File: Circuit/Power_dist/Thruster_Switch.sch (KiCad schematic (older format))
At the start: 11 parts, among them P1 XT60, P2 XT60, P3 XT60, P4 XT60, Q1 IPD90P03P4L

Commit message: edit sch and add pcix16
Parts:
- removed P2, P3, P4: XT60, zeabus:XT60, symbol XT60
- Q1: footprint TO_SOT_Packages_SMD:TO-252-2Lead -> TO_SOT_Packages_SMD:TO-252-2
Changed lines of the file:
@@
 EESchema Schematic File Version 2
+LIBS:Power_Distributor-rescue
 LIBS:power
 LIBS:device
@@
 LIBS:zeabus
 LIBS:ftdi
+LIBS:Power_Distributor-cache
 EELAYER 25 0
 EELAYER END
 $Descr A4 11693 8268
 encoding utf-8
-Sheet 6 9
+Sheet 2 9
 Title "Thruster Switch"
 Date "2017-04-06"
@@
 AR Path="/58E62AD5/58E019DD" Ref="P7"  Part="1"
 AR Path="/58E0048C/58E019DD" Ref="P11"  Part="1"
-F 0 "P11" H 6850 4450 50  0000 C CNN
+F 0 "P1" H 6850 4450 50  0000 C CNN
 F 1 "XT60" H 6850 4150 50  0000 C CNN
 F 2 "zeabus:XT60" H 6950 4050 60  0001 C CNN
@@
 AR Path="/58E62AD5/58E01A68" Ref="R12"  Part="1"
 AR Path="/58E0048C/58E01A68" Ref="R15"  Part="1"
-F 0 "R15" V 6330 4150 50  0000 C CNN
+F 0 "R3" V 6330 4150 50  0000 C CNN
 F 1 "10k" V 6250 4150 50  0000 C CNN
 F 2 "Resistors_SMD:R_0603" V 6180 4150 50  0001 C CNN
@@
 AR Path="/58E62AD5/58E01A8B" Ref="D8"  Part="1"
 AR Path="/58E0048C/58E01A8B" Ref="D10"  Part="1"
-F 0 "D10" H 6200 4675 50  0000 L CNN
+F 0 "D2" H 6200 4675 50  0000 L CNN
 F 1 "LED_Small" H 6075 4450 50  0000 L CNN
 F 2 "LEDs:LED_0603" V 6250 4550 50  0001 C CNN
@@
 AR Path="/58E62AD5/58E01FA8" Ref="R10"  Part="1"
 AR Path="/58E0048C/58E01FA8" Ref="R13"  Part="1"
-F 0 "R13" V 5630 2500 50  0000 C CNN
+F 0 "R1" V 5630 2500 50  0000 C CNN
 F 1 "10k" V 5550 2500 50  0000 C CNN
 F 2 "Resistors_SMD:R_0603" V 5480 2500 50  0001 C CNN
@@
 AR Path="/58E62AD5/58E01FFB" Ref="R11"  Part="1"
 AR Path="/58E0048C/58E01FFB" Ref="R14"  Part="1"
-F 0 "R14" V 5630 3050 50  0000 C CNN
+F 0 "R2" V 5630 3050 50  0000 C CNN
 F 1 "2.2k" V 5550 3050 50  0000 C CNN
 F 2 "Resistors_SMD:R_0603" V 5480 3050 50  0001 C CNN
@@
 $EndComp
 $Comp
-L GND #PWR011
+L GND #PWR020
 U 1 1 58E0369B
 P 6250 4800
-AR Path="/58E52973/58E0369B" Ref="#PWR011"  Part="1"
-AR Path="/58E62AD5/58E0369B" Ref="#PWR014"  Part="1"
-AR Path="/58E0048C/58E0369B" Ref="#PWR015"  Part="1"
-F 0 "#PWR015" H 6250 4550 50  0001 C CNN
+AR Path="/58E52973/58E0369B" Ref="#PWR020"  Part="1"
+AR Path="/58E62AD5/58E0369B" Ref="#PWR023"  Part="1"
+AR Path="/58E0048C/58E0369B" Ref="#PWR024"  Part="1"
+F 0 "#PWR024" H 6250 4550 50  0001 C CNN
 F 1 "GND" H 6250 4650 50  0000 C CNN
 F 2 "" H 6250 4800 50  0001 C CNN
@@
 Text HLabel 3700 3050 0    60   Input ~ 0
 Software_Switch
-$Comp
-L XT60 P2
-U 1 1 58E0D2A0
-P 7400 4300
-AR Path="/58E52973/58E0D2A0" Ref="P2"  Part="1"
-AR Path="/58E62AD5/58E0D2A0" Ref="P8"  Part="1"
-AR Path="/58E0048C/58E0D2A0" Ref="P12"  Part="1"
-F 0 "P12" H 7400 4450 50  0000 C CNN
-F 1 "XT60" H 7400 4150 50  0000 C CNN
-F 2 "zeabus:XT60" H 7500 4050 60  0001 C CNN
-F 3 "" H 7400 4300 60  0000 C CNN
-	1    7400 4300
-	1    0    0    -1
-$EndComp
-$Comp
-L XT60 P3
-U 1 1 58E0D2E8
-P 7950 4300
-AR Path="/58E52973/58E0D2E8" Ref="P3"  Part="1"
-AR Path="/58E62AD5/58E0D2E8" Ref="P9"  Part="1"
-AR Path="/58E0048C/58E0D2E8" Ref="P13"  Part="1"
-F 0 "P13" H 7950 4450 50  0000 C CNN
-F 1 "XT60" H 7950 4150 50  0000 C CNN
-F 2 "zeabus:XT60" H 8050 4050 60  0001 C CNN
-F 3 "" H 7950 4300 60  0000 C CNN
-	1    7950 4300
-	1    0    0    -1
-$EndComp
-$Comp
-L XT60 P4
-U 1 1 58E0D33F
-P 8500 4300
-AR Path="/58E52973/58E0D33F" Ref="P4"  Part="1"
-AR Path="/58E62AD5/58E0D33F" Ref="P10"  Part="1"
-AR Path="/58E0048C/58E0D33F" Ref="P14"  Part="1"
-F 0 "P14" H 8500 4450 50  0000 C CNN
-F 1 "XT60" H 8500 4150 50  0000 C CNN
-F 2 "zeabus:XT60" H 8600 4050 60  0001 C CNN
-F 3 "" H 8500 4300 60  0000 C CNN
-	1    8500 4300
-	1    0    0    -1
-$EndComp
 $Comp
 L Fuse F1
@@
 AR Path="/58E62AD5/58E4FE30" Ref="F4"  Part="1"
 AR Path="/58E0048C/58E4FE30" Ref="F5"  Part="1"
-F 0 "F5" V 6330 3550 50  0000 C CNN
+F 0 "F1" V 6330 3550 50  0000 C CNN
 F 1 "Fuse" V 6175 3550 50  0000 C CNN
 F 2 "zeabus:FUSE_AUTO" V 6180 3550 50  0001 C CNN
@@
 $EndComp
 Wire Wire Line
-	6250 3850 8300 3850
-Wire Wire Line
 	6650 3850 6650 4250
 Connection ~ 6250 3850
@@
 	5250 2500 5400 2500
 Connection ~ 5250 3050
-Wire Wire Line
-	8300 3850 8300 4250
 Connection ~ 6650 3850
-Wire Wire Line
-	8300 4750 8300 4350
-Wire Wire Line
-	7200 4250 7200 3850
-Connection ~ 7200 3850
-Wire Wire Line
-	7750 4250 7750 3850
-Connection ~ 7750 3850
 Wire Wire Line
 	6250 4450 6250 4300
 Connection ~ 6650 4750
-Wire Wire Line
-	7750 4750 7750 4350
-Connection ~ 7750 4750
-Wire Wire Line
-	7200 4750 7200 4350
-Connection ~ 7200 4750
 Wire Wire Line
 	6250 4650 6250 4800
@@
 AR Path="/58E62AD5/58E51C6A" Ref="Q4"  Part="1"
 AR Path="/58E0048C/58E51C6A" Ref="Q5"  Part="1"
-F 0 "Q5" H 6350 3100 50  0000 L CNN
+F 0 "Q1" H 6350 3100 50  0000 L CNN
 F 1 "IPD90P03P4L" H 6350 3000 50  0000 L CNN
-F 2 "TO_SOT_Packages_SMD:TO-252-2Lead" H 6350 3150 50  0001 C CNN
+F 2 "TO_SOT_Packages_SMD:TO-252-2" H 6350 3150 50  0001 C CNN
 F 3 "" H 6150 3050 50  0001 C CNN
 	1    6150 3050
@@
 AR Path="/58E62AD5/58E6427A" Ref="D7"  Part="1"
 AR Path="/58E0048C/58E6427A" Ref="D9"  Part="1"
-F 0 "D9" H 5850 2850 50  0000 C CNN
+F 0 "D1" H 5850 2850 50  0000 C CNN
 F 1 "BZX585-C12" H 5850 2650 50  0000 C CNN
 F 2 "Diodes_SMD:D_SOD-523" H 5850 2750 50  0001 C CNN
@@
 	5850 2900 5850 3050
 Connection ~ 5850 3050
-Wire Wire Line
-	6250 4750 8300 4750
 Connection ~ 6250 4750
 Wire Wire Line
@@
 Wire Wire Line
 	3700 2300 6250 2300
+Wire Wire Line
+	6250 4750 6650 4750
+Wire Wire Line
+	6650 3850 6250 3850
 $EndSCHEMATC

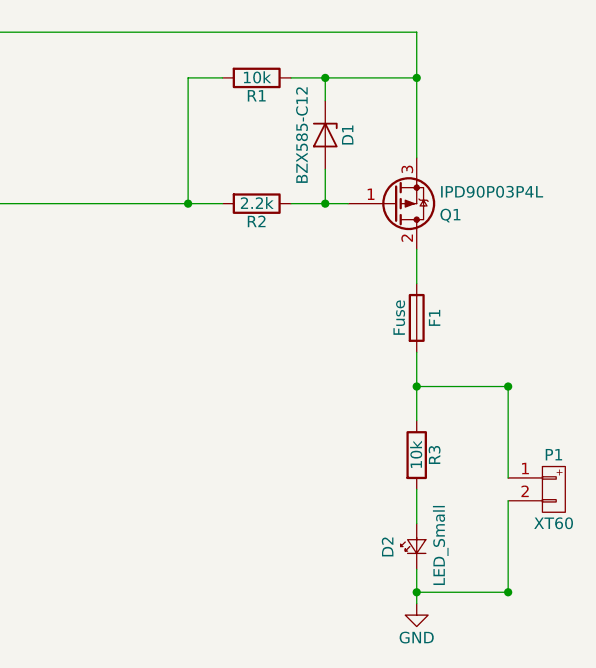
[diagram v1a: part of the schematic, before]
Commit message: delete fuses at thrusters and oring + add power on jumper
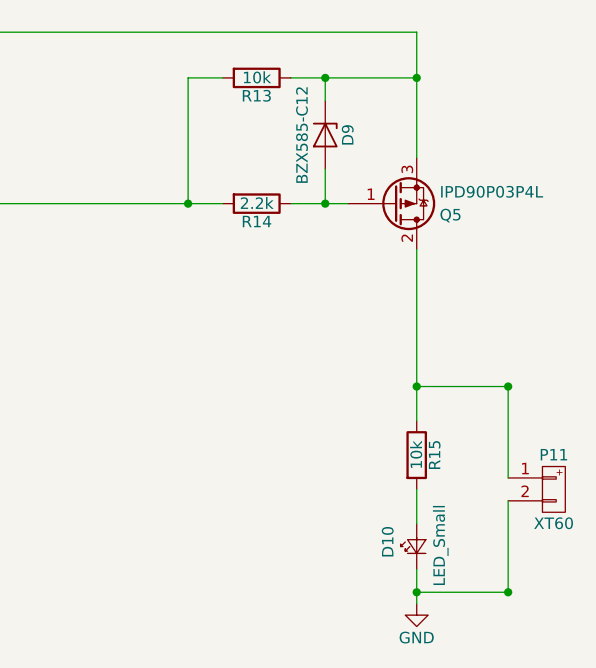
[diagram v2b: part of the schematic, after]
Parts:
- removed F1: Fuse, zeabus:FUSE_AUTO, symbol Fuse
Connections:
- net at P1.1 (P1), R3.1: now also Q1.2 (D)
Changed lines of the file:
@@
 $Descr A4 11693 8268
 encoding utf-8
-Sheet 2 9
+Sheet 5 8
 Title "Thruster Switch"
 Date "2017-04-06"
@@
 AR Path="/58E62AD5/58E019DD" Ref="P7"  Part="1"
 AR Path="/58E0048C/58E019DD" Ref="P11"  Part="1"
-F 0 "P1" H 6850 4450 50  0000 C CNN
+F 0 "P11" H 6850 4450 50  0000 C CNN
 F 1 "XT60" H 6850 4150 50  0000 C CNN
 F 2 "zeabus:XT60" H 6950 4050 60  0001 C CNN
@@
 AR Path="/58E62AD5/58E01A68" Ref="R12"  Part="1"
 AR Path="/58E0048C/58E01A68" Ref="R15"  Part="1"
-F 0 "R3" V 6330 4150 50  0000 C CNN
+F 0 "R15" V 6330 4150 50  0000 C CNN
 F 1 "10k" V 6250 4150 50  0000 C CNN
 F 2 "Resistors_SMD:R_0603" V 6180 4150 50  0001 C CNN
@@
 AR Path="/58E62AD5/58E01A8B" Ref="D8"  Part="1"
 AR Path="/58E0048C/58E01A8B" Ref="D10"  Part="1"
-F 0 "D2" H 6200 4675 50  0000 L CNN
+F 0 "D10" H 6200 4675 50  0000 L CNN
 F 1 "LED_Small" H 6075 4450 50  0000 L CNN
 F 2 "LEDs:LED_0603" V 6250 4550 50  0001 C CNN
@@
 AR Path="/58E62AD5/58E01FA8" Ref="R10"  Part="1"
 AR Path="/58E0048C/58E01FA8" Ref="R13"  Part="1"
-F 0 "R1" V 5630 2500 50  0000 C CNN
+F 0 "R13" V 5630 2500 50  0000 C CNN
 F 1 "10k" V 5550 2500 50  0000 C CNN
 F 2 "Resistors_SMD:R_0603" V 5480 2500 50  0001 C CNN
@@
 AR Path="/58E62AD5/58E01FFB" Ref="R11"  Part="1"
 AR Path="/58E0048C/58E01FFB" Ref="R14"  Part="1"
-F 0 "R2" V 5630 3050 50  0000 C CNN
+F 0 "R14" V 5630 3050 50  0000 C CNN
 F 1 "2.2k" V 5550 3050 50  0000 C CNN
 F 2 "Resistors_SMD:R_0603" V 5480 3050 50  0001 C CNN
@@
 Text HLabel 3700 3050 0    60   Input ~ 0
 Software_Switch
-$Comp
-L Fuse F1
-U 1 1 58E4FE30
-P 6250 3550
-AR Path="/58E52973/58E4FE30" Ref="F1"  Part="1"
-AR Path="/58E62AD5/58E4FE30" Ref="F4"  Part="1"
-AR Path="/58E0048C/58E4FE30" Ref="F5"  Part="1"
-F 0 "F1" V 6330 3550 50  0000 C CNN
-F 1 "Fuse" V 6175 3550 50  0000 C CNN
-F 2 "zeabus:FUSE_AUTO" V 6180 3550 50  0001 C CNN
-F 3 "" H 6250 3550 50  0001 C CNN
-	1    6250 3550
-	1    0    0    -1
-$EndComp
 Wire Wire Line
 	6650 3850 6650 4250
@@
 	6250 4650 6250 4800
 Wire Wire Line
-	6250 3250 6250 3400
-Wire Wire Line
-	6250 3700 6250 4000
+	6250 3250 6250 4000
 $Comp
 L Q_PMOS_GDS Q1
@@
 AR Path="/58E62AD5/58E51C6A" Ref="Q4"  Part="1"
 AR Path="/58E0048C/58E51C6A" Ref="Q5"  Part="1"
-F 0 "Q1" H 6350 3100 50  0000 L CNN
+F 0 "Q5" H 6350 3100 50  0000 L CNN
 F 1 "IPD90P03P4L" H 6350 3000 50  0000 L CNN
 F 2 "TO_SOT_Packages_SMD:TO-252-2" H 6350 3150 50  0001 C CNN
@@
 AR Path="/58E62AD5/58E6427A" Ref="D7"  Part="1"
 AR Path="/58E0048C/58E6427A" Ref="D9"  Part="1"
-F 0 "D1" H 5850 2850 50  0000 C CNN
+F 0 "D9" H 5850 2850 50  0000 C CNN
 F 1 "BZX585-C12" H 5850 2650 50  0000 C CNN
 F 2 "Diodes_SMD:D_SOD-523" H 5850 2750 50  0001 C CNN

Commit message: component alignment on pcb
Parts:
- D2: footprint LEDs:LED_0603 -> LEDs:LED_0603_HandSoldering
- R1, R2, R3: footprint Resistors_SMD:R_0603 -> Resistors_SMD:R_0603_HandSoldering
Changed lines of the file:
@@
 F 0 "R15" V 6330 4150 50  0000 C CNN
 F 1 "10k" V 6250 4150 50  0000 C CNN
-F 2 "Resistors_SMD:R_0603" V 6180 4150 50  0001 C CNN
+F 2 "Resistors_SMD:R_0603_HandSoldering" V 6180 4150 50  0001 C CNN
 F 3 "" H 6250 4150 50  0001 C CNN
 	1    6250 4150
@@
 F 0 "D10" H 6200 4675 50  0000 L CNN
 F 1 "LED_Small" H 6075 4450 50  0000 L CNN
-F 2 "LEDs:LED_0603" V 6250 4550 50  0001 C CNN
+F 2 "LEDs:LED_0603_HandSoldering" V 6250 4550 50  0001 C CNN
 F 3 "" V 6250 4550 50  0001 C CNN
 	1    6250 4550
@@
 F 0 "R13" V 5630 2500 50  0000 C CNN
 F 1 "10k" V 5550 2500 50  0000 C CNN
-F 2 "Resistors_SMD:R_0603" V 5480 2500 50  0001 C CNN
+F 2 "Resistors_SMD:R_0603_HandSoldering" V 5480 2500 50  0001 C CNN
 F 3 "" H 5550 2500 50  0001 C CNN
 	1    5550 2500
@@
 F 0 "R14" V 5630 3050 50  0000 C CNN
 F 1 "2.2k" V 5550 3050 50  0000 C CNN
-F 2 "Resistors_SMD:R_0603" V 5480 3050 50  0001 C CNN
+F 2 "Resistors_SMD:R_0603_HandSoldering" V 5480 3050 50  0001 C CNN
 F 3 "" H 5550 3050 50  0001 C CNN
 	1    5550 3050
@@
 $EndComp
 $Comp
-L GND #PWR020
+L GND #PWR026
 U 1 1 58E0369B
 P 6250 4800
-AR Path="/58E52973/58E0369B" Ref="#PWR020"  Part="1"
+AR Path="/58E52973/58E0369B" Ref="#PWR026"  Part="1"
 AR Path="/58E62AD5/58E0369B" Ref="#PWR023"  Part="1"
-AR Path="/58E0048C/58E0369B" Ref="#PWR024"  Part="1"
-F 0 "#PWR024" H 6250 4550 50  0001 C CNN
+AR Path="/58E0048C/58E0369B" Ref="#PWR029"  Part="1"
+F 0 "#PWR029" H 6250 4550 50  0001 C CNN
 F 1 "GND" H 6250 4650 50  0000 C CNN
 F 2 "" H 6250 4800 50  0001 C CNN
